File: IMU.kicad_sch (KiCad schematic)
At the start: 7 parts, among them U301 LIS3MDLTR, U302 LSM6DSOXTR

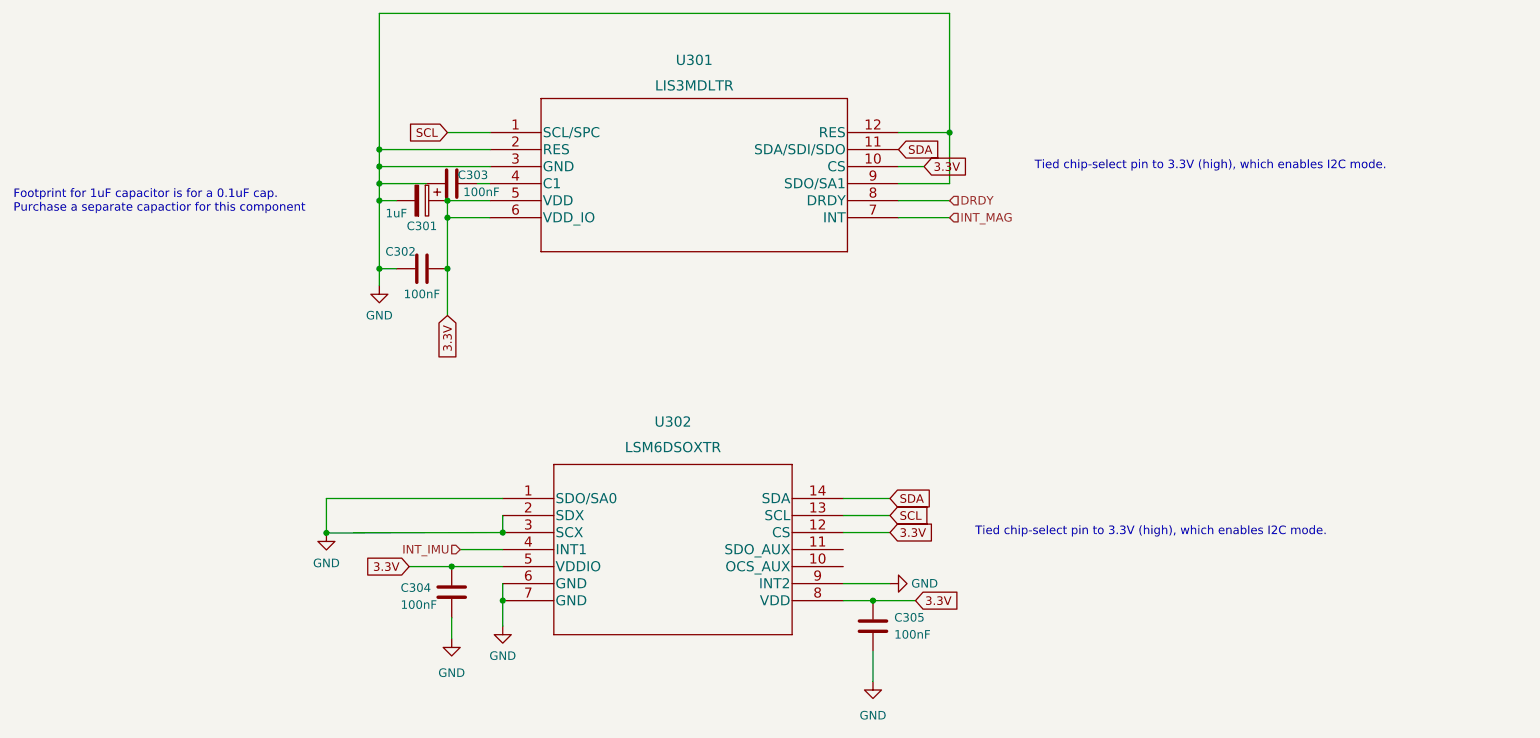
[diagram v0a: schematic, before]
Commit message: finished with schematics; fixed all errors in pcb
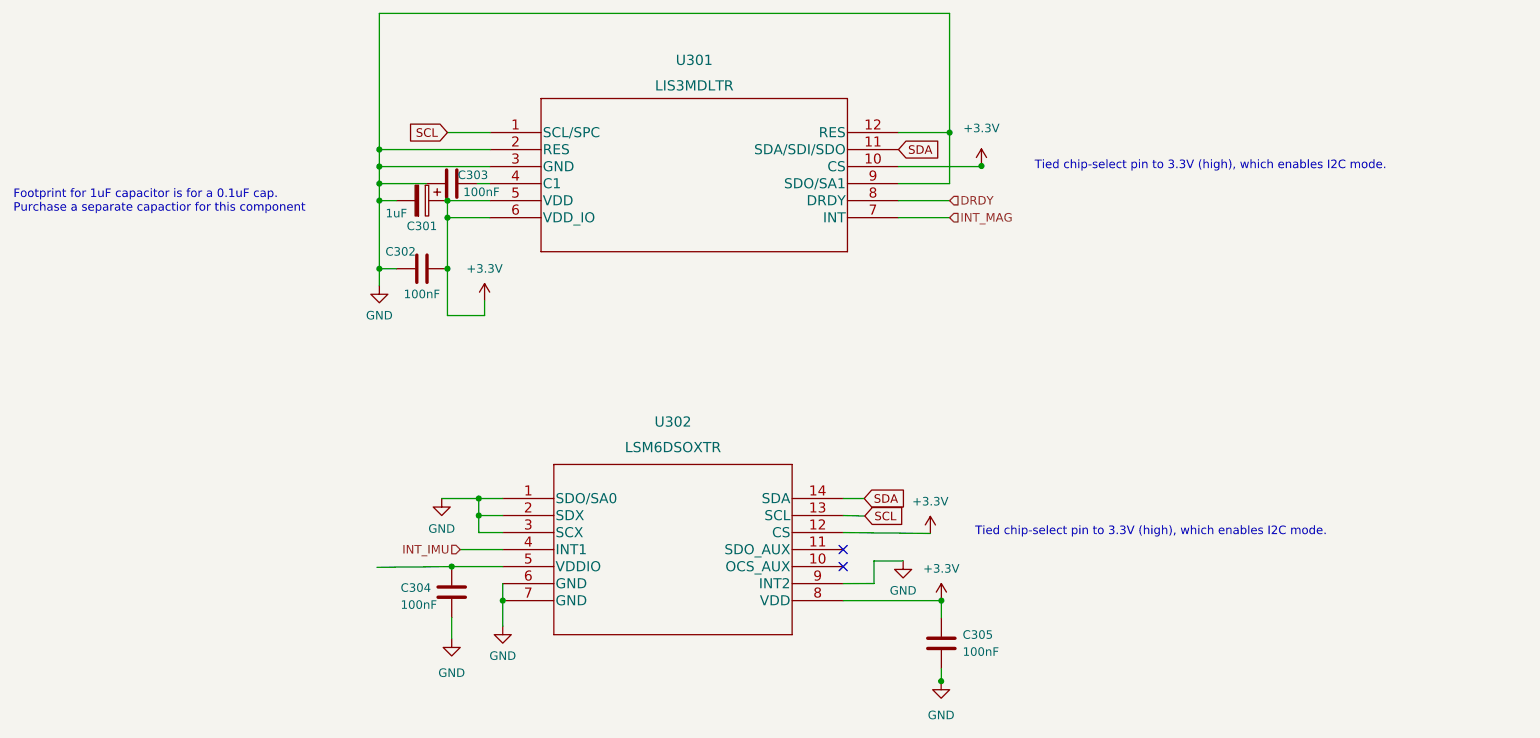
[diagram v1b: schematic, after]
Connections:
- net 3.3V renamed +3V3
- net +3V3: no longer C304.1, U302.5 (VDDIO)
- new net: C304.1, U302.5 (VDDIO)
- no-connect marks 0 -> 2
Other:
- moved on the sheet: C305
